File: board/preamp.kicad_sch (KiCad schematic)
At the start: 10 parts, among them U5 MAX4062

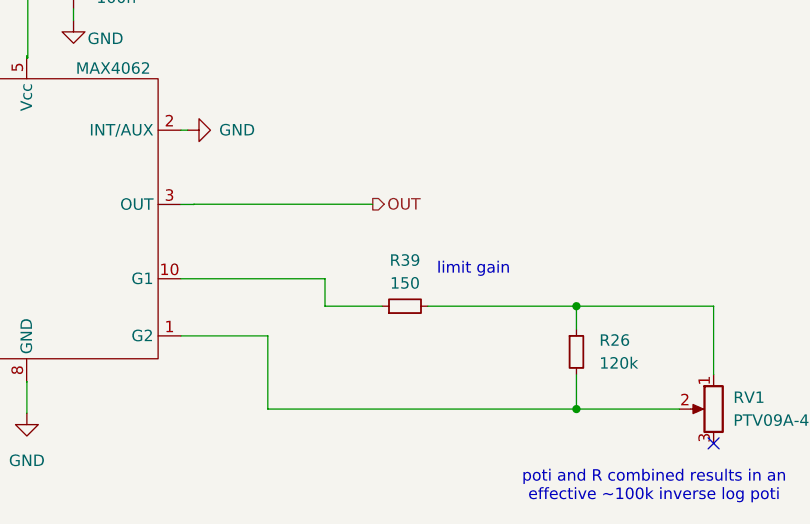
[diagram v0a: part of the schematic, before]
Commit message: correct connector positions, some silkscreen updates
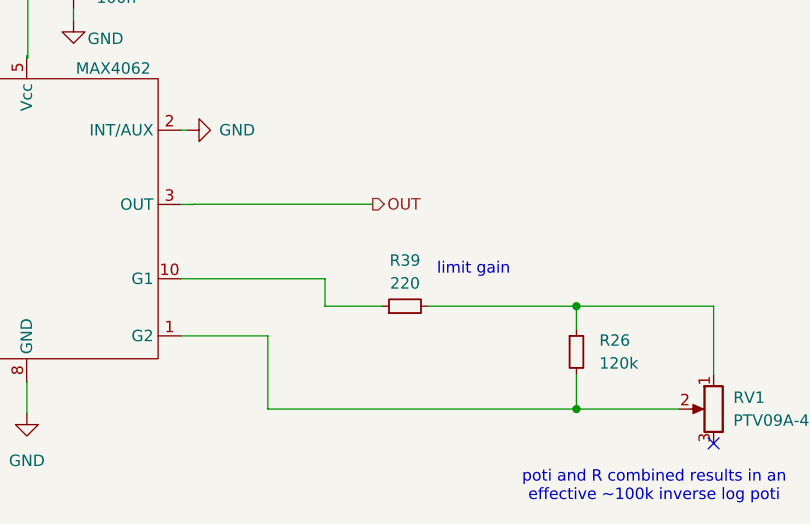
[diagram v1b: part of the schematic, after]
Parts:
- R39: value 150 -> 220
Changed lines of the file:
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@@
 			)
 		)
-		(property "Value" "150"
+		(property "Value" "220"
 			(at 222.25 85.09 90)
 			(effects

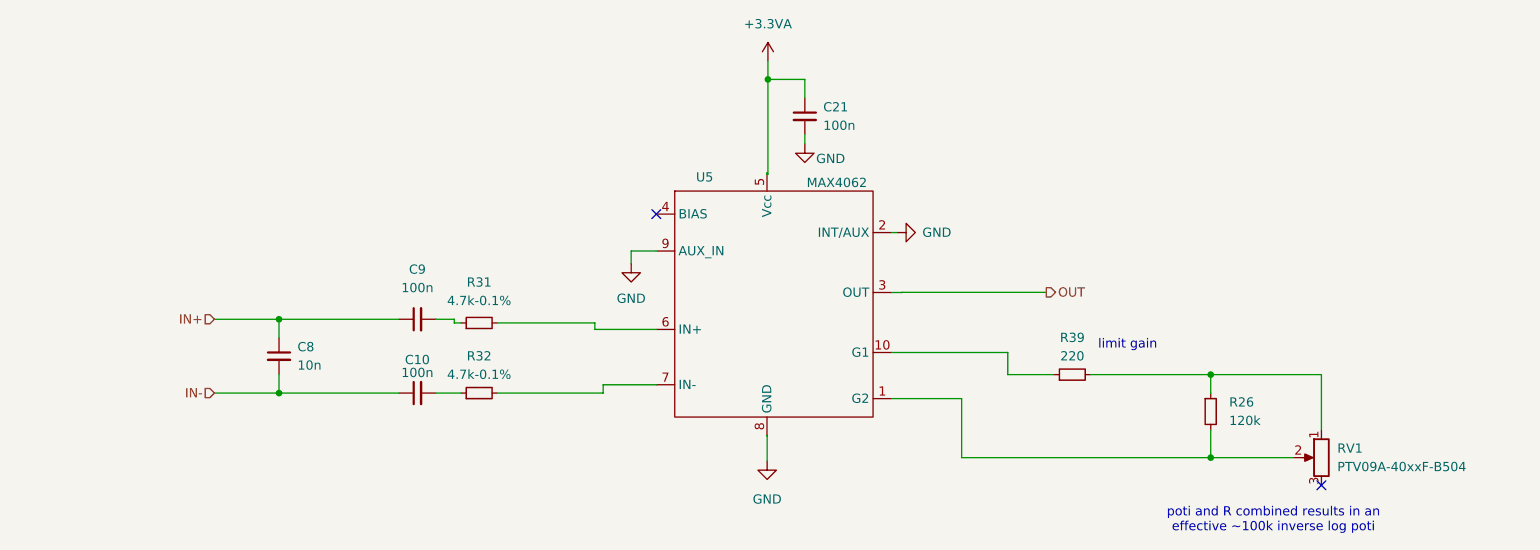
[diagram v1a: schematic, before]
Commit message: EMI improvements, allow PJ358 footprints, DRC fixes, poti changes
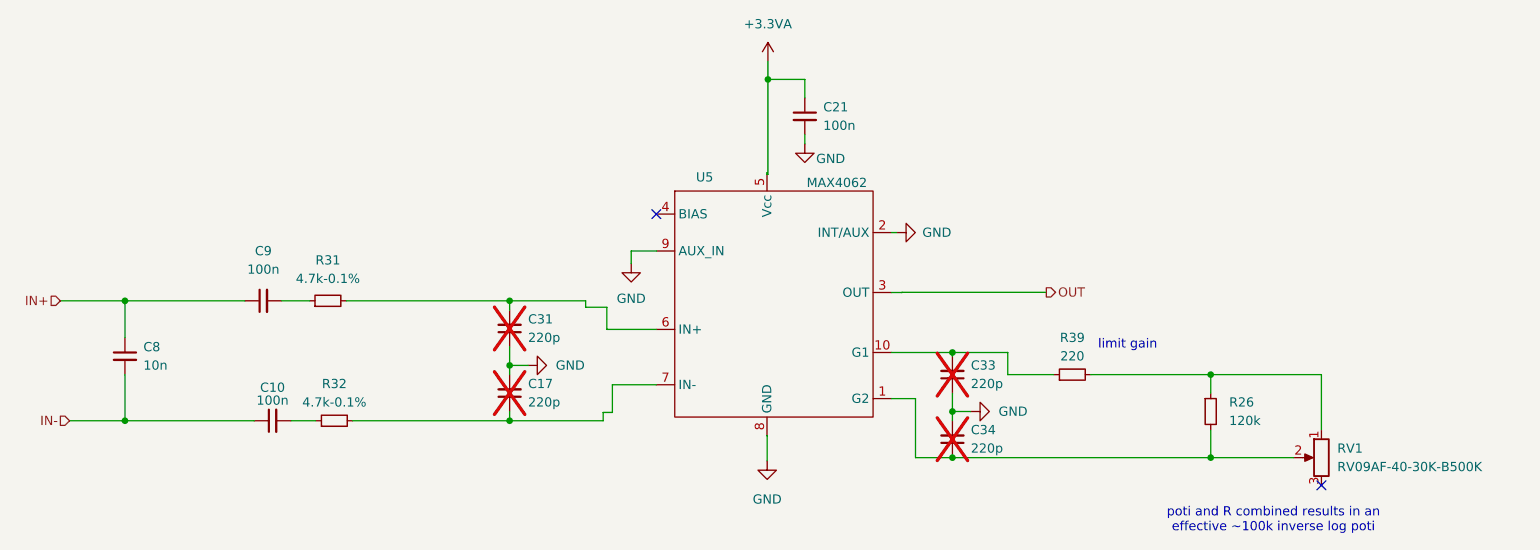
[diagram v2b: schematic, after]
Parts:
- added C17, C31, C33, C34: 220p, Capacitor_THT:C_Disc_D3.0mm_W2.0mm_P2.50mm, symbol Device:C_Small
- RV1: value PTV09A-40xxF-B504 -> RV09AF-40-30K-B500K
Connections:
- net GND: now also C17.2, C31.1, C33.1, C34.2
- net at R26.2, RV1.2, U5.1 (G2): now also C34.1
- net at R39.1, U5.10 (G1): now also C33.2
- net at R31.2, U5.6 (IN+): now also C31.2
- net at R32.2, U5.7 (IN-): now also C17.1
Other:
- moved on the sheet: C10, C8, C9, R31, R32

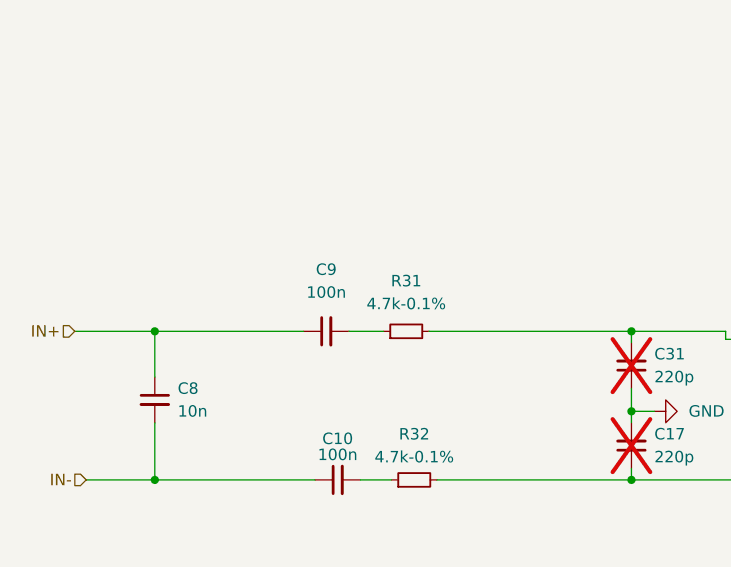
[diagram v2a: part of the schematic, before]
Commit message: reduce BOM and more mechanical stable PJ358
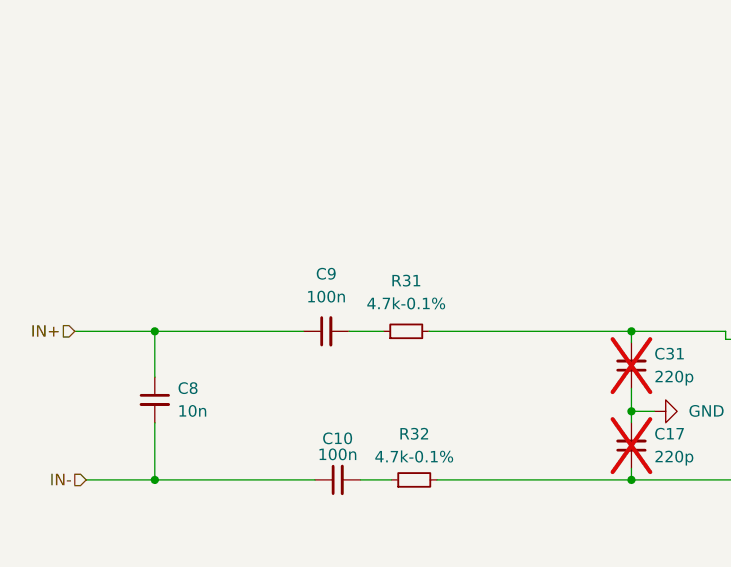
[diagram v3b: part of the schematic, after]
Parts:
- C10, C9: footprint Capacitor_THT:C_Disc_D5.1mm_W3.2mm_P5.00mm -> Capacitor_THT:C_Disc_D4.3mm_W1.9mm_P5.00mm
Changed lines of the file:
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@@
 			)
 		)
-		(property "Footprint" "Capacitor_THT:C_Disc_D5.1mm_W3.2mm_P5.00mm"
+		(property "Footprint" "Capacitor_THT:C_Disc_D4.3mm_W1.9mm_P5.00mm"
 			(at 112.141 93.98 0)
 			(effects
@@
 		(fields_autoplaced yes)
 		(property "Reference" "C9"
-			(at 110.8773 70.612 90)
+			(at 110.8773 71.12 90)
 			(effects
 				(font
@@
 		)
 		(property "Value" "100n"
-			(at 110.8773 73.152 90)
+			(at 110.8773 73.66 90)
 			(effects
 				(font
@@
 			)
 		)
-		(property "Footprint" "Capacitor_THT:C_Disc_D5.1mm_W3.2mm_P5.00mm"
+		(property "Footprint" "Capacitor_THT:C_Disc_D4.3mm_W1.9mm_P5.00mm"
 			(at 110.871 77.47 0)
 			(effects

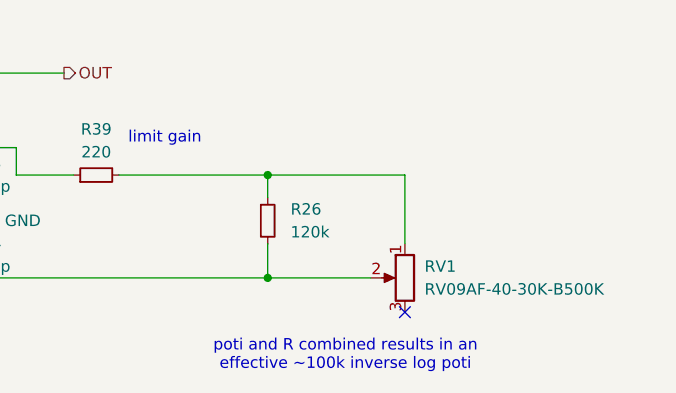
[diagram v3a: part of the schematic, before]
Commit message: poti: rotate 180deg and switch back to 100k with a reverse audio taper
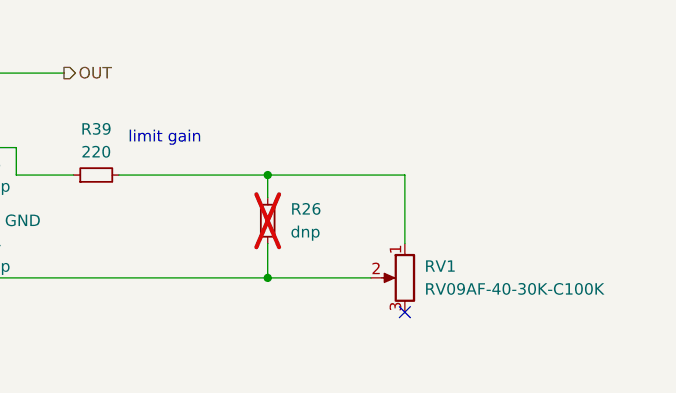
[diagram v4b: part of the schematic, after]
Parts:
- R26: value 120k -> dnp; now not fitted
- RV1: value RV09AF-40-30K-B500K -> RV09AF-40-30K-C100K
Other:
- note removed: "poti and R combined results in an effective ~100k inverse log poti"
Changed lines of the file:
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@@
 		)
 	)
-	(text "poti and R combined results in an\neffective ~100k inverse log poti"
-		(exclude_from_sim no)
-		(at 249.936 107.696 0)
+	(hierarchical_label "OUT"
+		(shape output)
+		(at 218.6686 76.3016 0)
+		(fields_autoplaced yes)
 		(effects
 			(font
 				(size 1.27 1.27)
 			)
-		)
-	)
-	(hierarchical_label "OUT"
-		(shape output)
-		(at 218.6686 76.3016 0)
+			(justify left)
+		)
+	)
+	(hierarchical_label "IN+"
+		(shape input)
+		(at 82.931 77.47 180)
 		(fields_autoplaced yes)
 		(effects
@@
 				(size 1.27 1.27)
 			)
-			(justify left)
-		)
-	)
-	(hierarchical_label "IN+"
+			(justify right)
+		)
+	)
+	(hierarchical_label "IN-"
 		(shape input)
-		(at 82.931 77.47 180)
+		(at 84.201 93.98 180)
 		(fields_autoplaced yes)
 		(effects
@@
 		)
 	)
-	(hierarchical_label "IN-"
-		(shape input)
-		(at 84.201 93.98 180)
-		(fields_autoplaced yes)
-		(effects
-			(font
-				(size 1.27 1.27)
-			)
-			(justify right)
-		)
-	)
 	(symbol
 		(lib_id "Device:R_Small")
@@
 		(in_bom no)
 		(on_board yes)
-		(dnp no)
+		(dnp yes)
 		(fields_autoplaced yes)
 		(property "Reference" "R26"
@@
 			)
 		)
-		(property "Value" "120k"
+		(property "Value" "dnp"
 			(at 243.84 93.9799 0)
 			(effects
@@
 			)
 		)
-		(property "Value" "RV09AF-40-30K-B500K"
+		(property "Value" "RV09AF-40-30K-C100K"
 			(at 258.7244 100.33 0)
 			(effects

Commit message: incoorperate matthias feedback
- clearances
- opamp swap
- shorter traces
- ...
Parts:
- R39: footprint Resistor_THT:R_Axial_DIN0207_L6.3mm_D2.5mm_P10.16mm_Horizontal -> Resistor_THT:R_Axial_DIN0204_L3.6mm_D1.6mm_P5.08mm_Horizontal
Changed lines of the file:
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@@
 			)
 		)
-		(property "Footprint" "Resistor_THT:R_Axial_DIN0207_L6.3mm_D2.5mm_P10.16mm_Horizontal"
+		(property "Footprint" "Resistor_THT:R_Axial_DIN0204_L3.6mm_D1.6mm_P5.08mm_Horizontal"
 			(at 222.25 87.63 0)
 			(effects

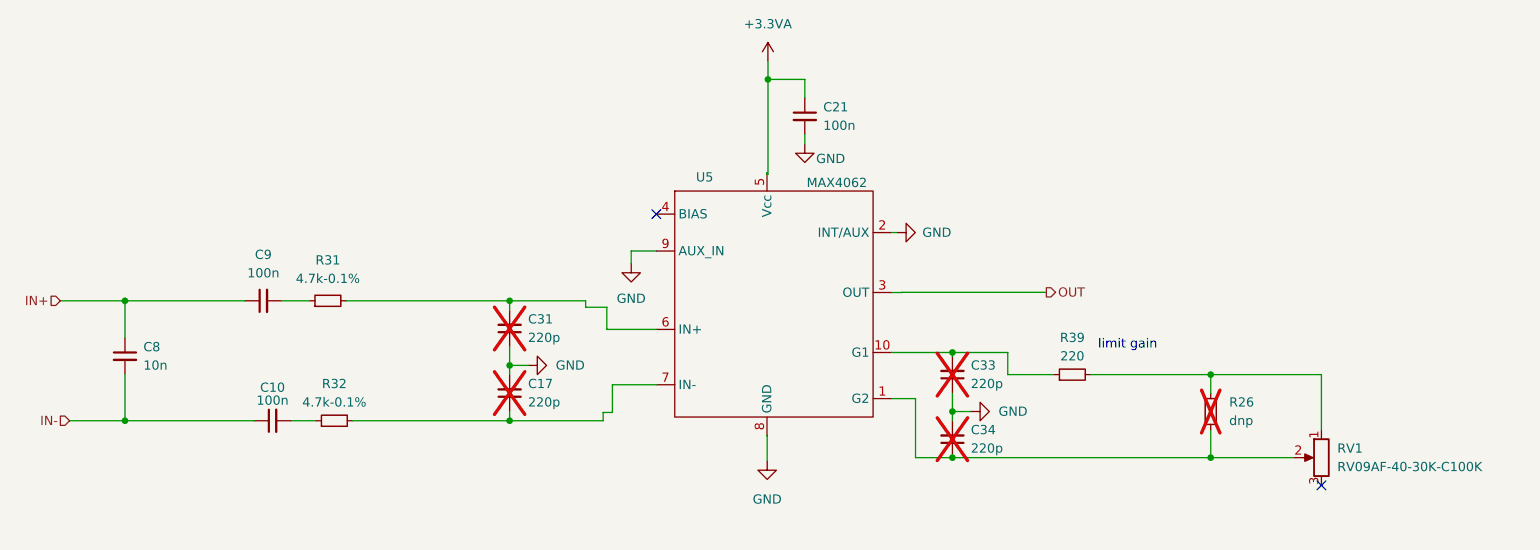
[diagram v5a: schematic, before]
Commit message: add some spare capacitors for EMI tests
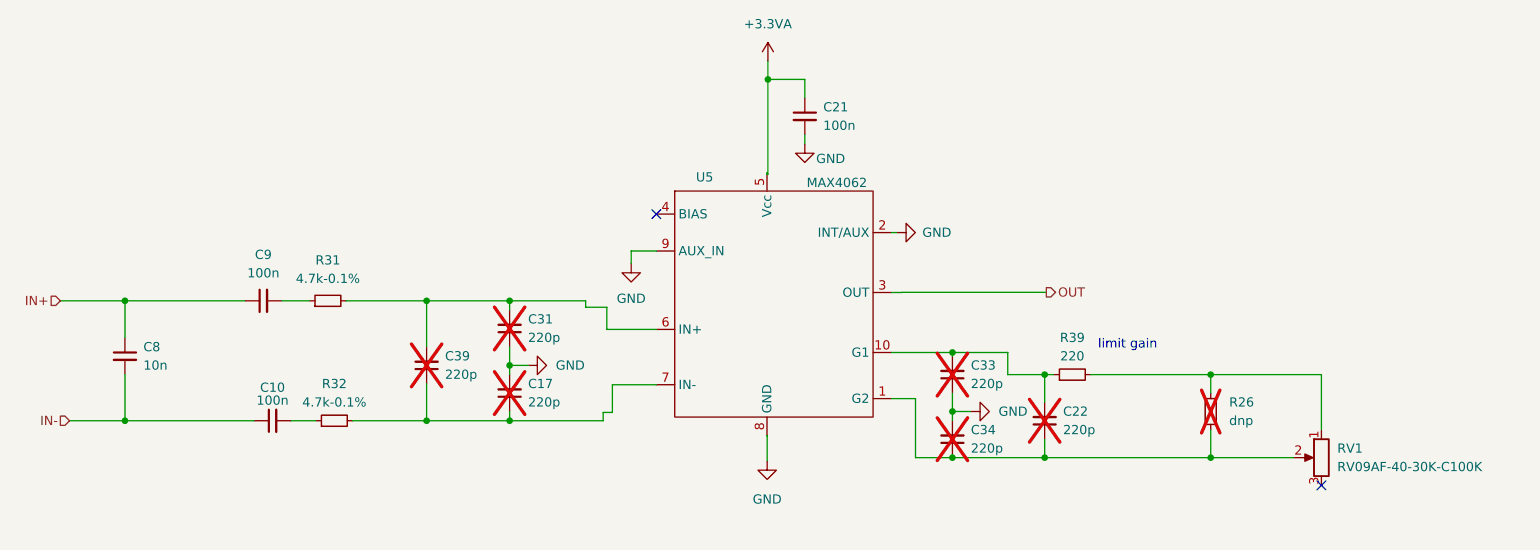
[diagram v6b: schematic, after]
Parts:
- added C22, C39: 220p, Capacitor_THT:C_Disc_D3.0mm_W2.0mm_P2.50mm, symbol Device:C_Small
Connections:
- net at C34.1, R26.2, RV1.2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: now also C22.1
- net at C31.2, R31.2, U5.6 (IN+): now also C39.2
- net at C17.1, R32.2, U5.7 (IN-): now also C39.1
- net at C33.2, R39.1, U5.10 (G1): now also C22.2

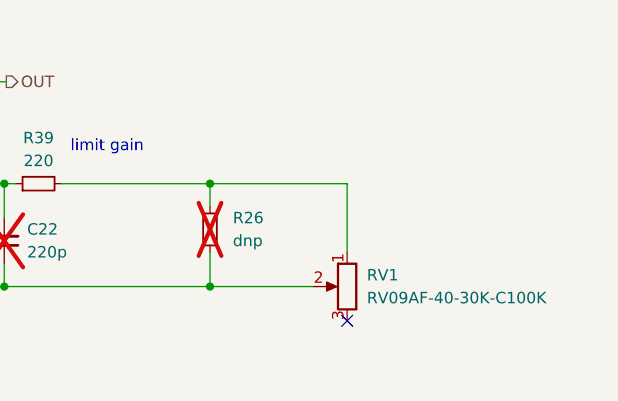
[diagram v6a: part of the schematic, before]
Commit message: more EMI protection C's and poti inverting jumper
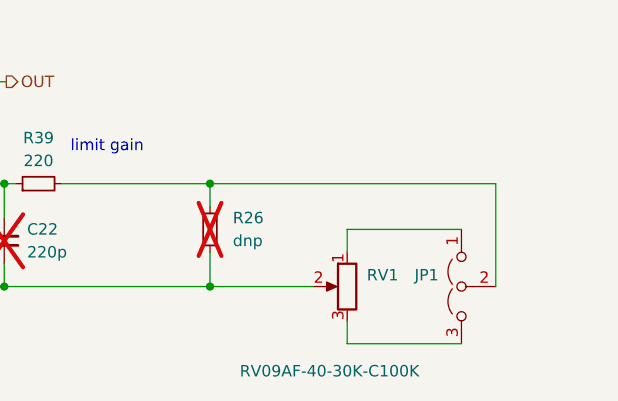
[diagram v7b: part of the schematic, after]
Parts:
- added JP1: ~, Jumper:SolderJumper-3_P1.3mm_Open_RoundedPad1.0x1.5mm_NumberLabels, symbol Jumper:Jumper_3_Open
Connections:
- net at R26.1, R39.2: now also JP1.2 (C); no longer RV1.1
- net at RV1.3: now also JP1.3 (B)
- new net: JP1.1 (A), RV1.1
- no-connect marks 2 -> 1
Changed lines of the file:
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@@
-	)
-	(no_connect
-		(at 256.54 102.87)
 	)
 	(no_connect
@@
 	(wire
 		(pts
+			(xy 269.24 105.41) (xy 256.54 105.41)
+		)
+		(stroke
+			(width 0)
+			(type default)
+		)
+	)
+	(wire
+		(pts
 			(xy 144.78 86.36) (xy 147.32 86.36)
 		)
@@
 	(wire
 		(pts
-			(xy 241.3 87.63) (xy 256.54 87.63)
+			(xy 241.3 87.63) (xy 273.05 87.63)
 		)
 		(stroke
@@
 	(wire
 		(pts
-			(xy 256.54 87.63) (xy 256.54 95.25)
-		)
-		(stroke
-			(width 0)
-			(type default)
-		)
-	)
-	(wire
-		(pts
 			(xy 180.34 60.0456) (xy 180.213 60.0456)
 		)
@@
 	(wire
 		(pts
+			(xy 256.54 105.41) (xy 256.54 102.87)
+		)
+		(stroke
+			(width 0)
+			(type default)
+		)
+	)
+	(wire
+		(pts
 			(xy 155.2448 78.359) (xy 158.1658 78.359)
 		)
@@
 	(wire
 		(pts
+			(xy 256.54 95.25) (xy 256.54 92.71)
+		)
+		(stroke
+			(width 0)
+			(type default)
+		)
+	)
+	(wire
+		(pts
 			(xy 123.19 93.98) (xy 133.35 93.98)
+		)
+		(stroke
+			(width 0)
+			(type default)
+		)
+	)
+	(wire
+		(pts
+			(xy 273.05 99.06) (xy 273.05 87.63)
+		)
+		(stroke
+			(width 0)
+			(type default)
+		)
+	)
+	(wire
+		(pts
+			(xy 256.54 92.71) (xy 269.24 92.71)
 		)
 		(stroke
@@
 		)
 		(property "Value" "RV09AF-40-30K-C100K"
-			(at 258.7244 100.33 0)
+			(at 244.602 108.458 0)
 			(effects
 				(font
@@
 					(unit 1)
 				)
+			)
+		)
+	)
+	(symbol
+		(lib_id "Jumper:Jumper_3_Open")
+		(at 269.24 99.06 90)
+		(mirror x)
+		(unit 1)
+		(exclude_from_sim yes)
+		(in_bom no)
+		(on_board yes)
+		(dnp no)
+		(property "Reference" "JP1"
+			(at 266.7 97.7899 90)
+			(effects
+				(font
+					(size 1.27 1.27)
+				)
+				(justify left)
+			)
+		)
+		(property "Value" "~"
+			(at 266.7 100.3299 90)
+			(effects
+				(font
+					(size 1.27 1.27)
+				)
+				(justify left)
+			)
+		)
+		(property "Footprint" "Jumper:SolderJumper-3_P1.3mm_Open_RoundedPad1.0x1.5mm_NumberLabels"
+			(at 269.24 99.06 0)
+			(effects
+				(font
+					(size 1.27 1.27)
+				)
+				(hide yes)
+			)
+		)
+		(property "Datasheet" "~"
+			(at 269.24 99.06 0)
+			(effects
+				(font
+					(size 1.27 1.27)
+				)
+				(hide yes)
+			)
+		)
+		(property "Description" "Jumper, 3-pole, both open"
+			(at 269.24 99.06 0)
+			(effects
+				(font
+					(size 1.27 1.27)
+				)
+				(hide yes)
+			)
+		)
+		(pin "3"
+		)
+		(pin "2"
+		)
+		(pin "1"
+		)
+		(instances
+			(project "spider2"
+				(path "/31073f88-a990-4ecc-8ab9-bb6b56c98e1e/ef17f1e3-6d4b-48c3-ada3-a0af083f4146"
+					(reference "JP1")
+					(unit 1)
+				)
+				(path "/31073f88-a990-4ecc-8ab9-bb6b56c98e1e/5a710a45-03d0-4177-b57a-0573a00e8cb4"
+					(reference "JP2")
+					(unit 1)
+				)
